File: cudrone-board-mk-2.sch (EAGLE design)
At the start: 58 parts, among them Q1 BSS138, U1 EDISON_CONNECTOR_FULLMOUNTING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, U2 FTS31XS-U, U4 TPS62065, U5 USD-SOCKETNEW, U6 TXB0108, U8 PCA9306, U9 MIC5205

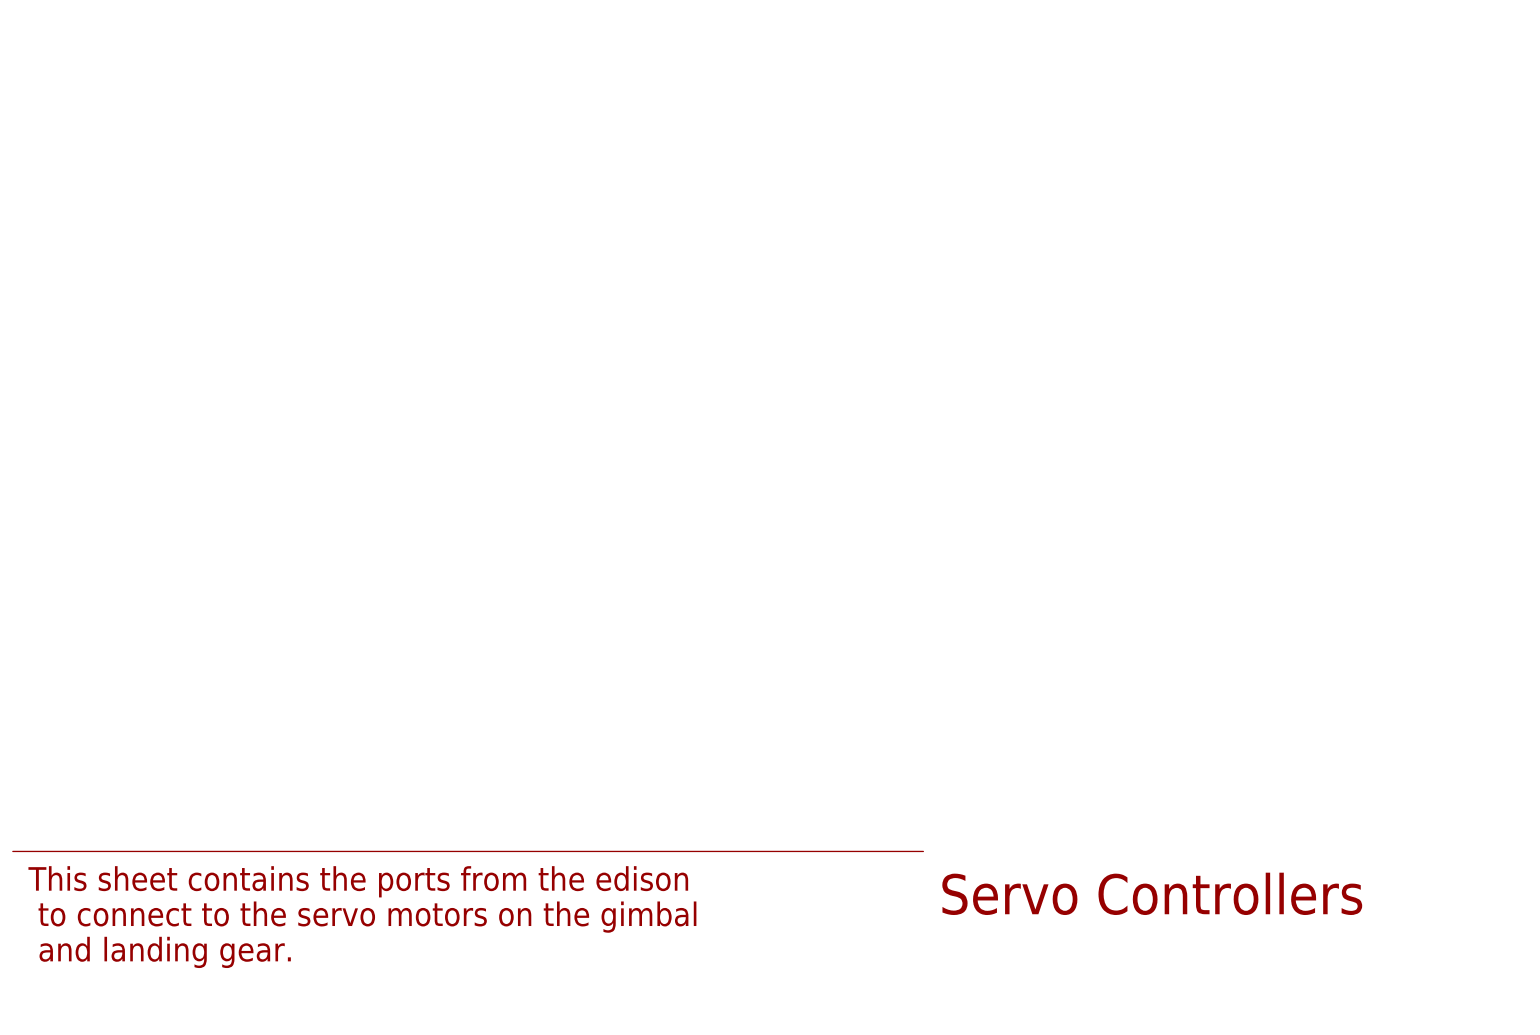
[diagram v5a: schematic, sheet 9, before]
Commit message: Added connectors to schematic
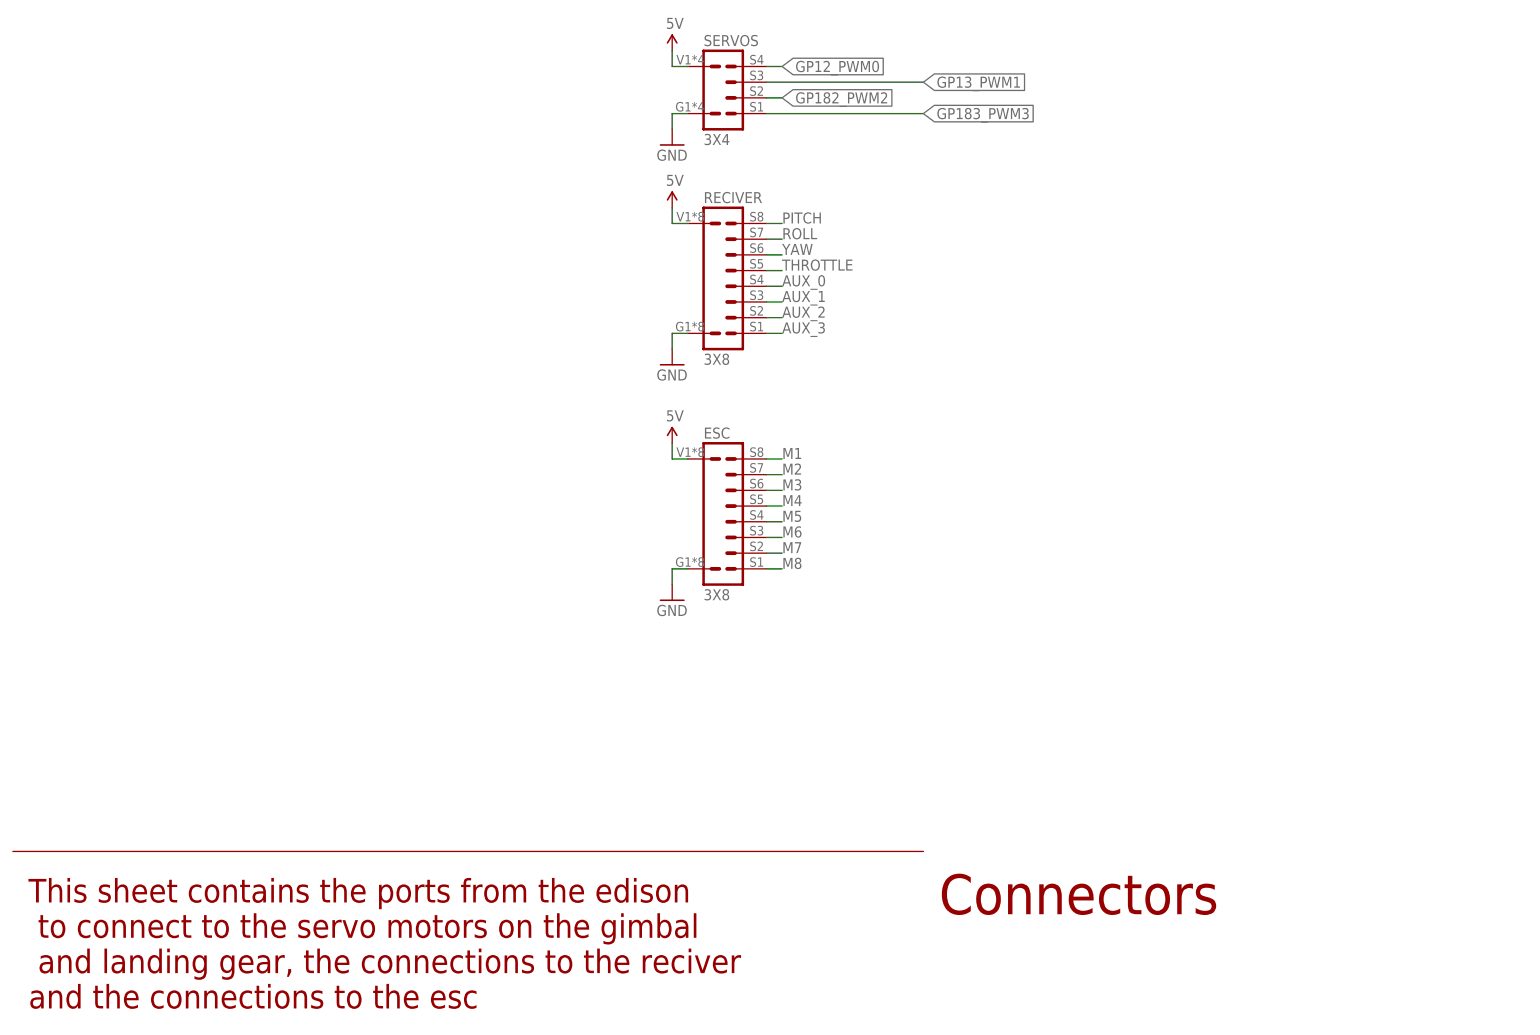
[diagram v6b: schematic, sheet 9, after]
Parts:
- added ESC, RECIVER: 3X8, Drone_Connectors:3X8
- added SERVOS: 3X4, Drone_Connectors:3X4
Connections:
- new net AUX_0: RECIVER.4
- new net AUX_1: RECIVER.3
- new net AUX_2: RECIVER.2
- new net AUX_3: RECIVER.1
- new net M1: ESC.8
- new net M2: ESC.7
- new net M3: ESC.6
- new net M4: ESC.5
- new net M5: ESC.4
- new net M6: ESC.3
- new net M7: ESC.2
- new net M8: ESC.1
- new net PITCH: RECIVER.8
- new net ROLL: RECIVER.7
- new net THROTTLE: RECIVER.5
- new net YAW: RECIVER.6
- net 5V: now also ESC.V, RECIVER.V, SERVOS.V
- net GND: now also ESC.G, RECIVER.G, SERVOS.G
- net GP12_PWM0: now also SERVOS.S4
- net GP13_PWM1: now also SERVOS.S3
- net GP182_PWM2: now also SERVOS.S2
- net GP183_PWM3: now also SERVOS.S1
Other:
- note added: "Connectors"
- note added: "This sheet contains the ports from the edison to connect to the servo motors on the gimbal and landing gear, the connections to the reciver and the connections to the esc"
- note removed: "Servo Controllers"
- note removed: "This sheet contains the ports from the edison to connect to the servo motors on the gimbal and landing gear."
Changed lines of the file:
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@@
 <layer number="113" name="IDFDebug" color="7" fill="1" visible="yes" active="yes"/>
 <layer number="114" name="Badge_Outline" color="11" fill="1" visible="no" active="no"/>
+<layer number="115" name="ReferenceISLANDS" color="7" fill="1" visible="yes" active="yes"/>
 <layer number="116" name="Patch_BOT" color="9" fill="4" visible="yes" active="yes"/>
 <layer number="118" name="Rect_Pads" color="7" fill="1" visible="yes" active="yes"/>
@@
 <part name="SUPPLY22" library="SparkFun-Aesthetics" deviceset="1.8V" device=""/>
 <part name="SUPPLY23" library="SparkFun-Aesthetics" deviceset="1.8V" device=""/>
+<part name="SERVOS" library="Drone_Connectors" deviceset="3X4" device=""/>
+<part name="RECIVER" library="Drone_Connectors" deviceset="3X8" device=""/>
+<part name="ESC" library="Drone_Connectors" deviceset="3X8" device=""/>
+<part name="SUPPLY24" library="SparkFun-Aesthetics" deviceset="5V" device=""/>
+<part name="SUPPLY25" library="SparkFun-Aesthetics" deviceset="5V" device=""/>
+<part name="SUPPLY26" library="SparkFun-Aesthetics" deviceset="5V" device=""/>
+<part name="GND34" library="SparkFun-Aesthetics" deviceset="GND" device=""/>
+<part name="GND35" library="SparkFun-Aesthetics" deviceset="GND" device=""/>
+<part name="GND36" library="SparkFun-Aesthetics" deviceset="GND" device=""/>
 </parts>
 <sheets>
@@
 <sheet>
 <plain>
-<text x="149.86" y="25.4" size="6.4516" layer="94">Servo Controllers</text>
+<text x="149.86" y="25.4" size="6.4516" layer="94">Connectors</text>
 <wire x1="147.32" y1="35.56" x2="0" y2="35.56" width="0.1524" layer="94"/>
-<text x="2.54" y="17.78" size="3.81" layer="94">This sheet contains the ports from the edison
+<text x="2.54" y="10.16" size="3.81" layer="94">This sheet contains the ports from the edison
  to connect to the servo motors on the gimbal
- and landing gear.</text>
+ and landing gear, the connections to the reciver
+and the connections to the esc</text>
 </plain>
 <instances>
 <instance part="FRAME9" gate="G$1" x="0" y="0"/>
 <instance part="FRAME9" gate="G$2" x="147.32" y="0"/>
+<instance part="SERVOS" gate="G$1" x="114.3" y="160.02"/>
+<instance part="RECIVER" gate="G$1" x="114.3" y="129.54"/>
+<instance part="ESC" gate="G$1" x="114.3" y="91.44"/>
+<instance part="SUPPLY24" gate="G$1" x="106.68" y="165.1"/>
+<instance part="SUPPLY25" gate="G$1" x="106.68" y="139.7"/>
+<instance part="SUPPLY26" gate="G$1" x="106.68" y="101.6"/>
+<instance part="GND34" gate="1" x="106.68" y="76.2"/>
+<instance part="GND35" gate="1" x="106.68" y="114.3"/>
+<instance part="GND36" gate="1" x="106.68" y="149.86"/>
 </instances>
 <busses>
 </busses>
 <nets>
+<net name="GND" class="0">
+<segment>
+<pinref part="GND36" gate="1" pin="GND"/>
+<wire x1="106.68" y1="152.4" x2="106.68" y2="154.94" width="0.1524" layer="91"/>
+<pinref part="SERVOS" gate="G$1" pin="G"/>
+<wire x1="106.68" y1="154.94" x2="109.22" y2="154.94" width="0.1524" layer="91"/>
+</segment>
+<segment>
+<pinref part="GND35" gate="1" pin="GND"/>
+<wire x1="106.68" y1="116.84" x2="106.68" y2="119.38" width="0.1524" layer="91"/>
+<pinref part="RECIVER" gate="G$1" pin="G"/>
+<wire x1="106.68" y1="119.38" x2="109.22" y2="119.38" width="0.1524" layer="91"/>
+</segment>
+<segment>
+<pinref part="GND34" gate="1" pin="GND"/>
+<wire x1="106.68" y1="78.74" x2="106.68" y2="81.28" width="0.1524" layer="91"/>
+<pinref part="ESC" gate="G$1" pin="G"/>
+<wire x1="106.68" y1="81.28" x2="109.22" y2="81.28" width="0.1524" layer="91"/>
+</segment>
+</net>
+<net name="5V" class="0">
+<segment>
+<pinref part="SUPPLY24" gate="G$1" pin="5V"/>
+<wire x1="106.68" y1="165.1" x2="106.68" y2="162.56" width="0.1524" layer="91"/>
+<pinref part="SERVOS" gate="G$1" pin="V"/>
+<wire x1="106.68" y1="162.56" x2="109.22" y2="162.56" width="0.1524" layer="91"/>
+</segment>
+<segment>
+<pinref part="SUPPLY25" gate="G$1" pin="5V"/>
+<wire x1="106.68" y1="139.7" x2="106.68" y2="137.16" width="0.1524" layer="91"/>
+<pinref part="RECIVER" gate="G$1" pin="V"/>
+<wire x1="106.68" y1="137.16" x2="109.22" y2="137.16" width="0.1524" layer="91"/>
+</segment>
+<segment>
+<pinref part="SUPPLY26" gate="G$1" pin="5V"/>
+<wire x1="106.68" y1="101.6" x2="106.68" y2="99.06" width="0.1524" layer="91"/>
+<pinref part="ESC" gate="G$1" pin="V"/>
+<wire x1="106.68" y1="99.06" x2="109.22" y2="99.06" width="0.1524" layer="91"/>
+</segment>
+</net>
+<net name="GP12_PWM0" class="0">
+<segment>
+<pinref part="SERVOS" gate="G$1" pin="S4"/>
+<wire x1="121.92" y1="162.56" x2="124.46" y2="162.56" width="0.1524" layer="91"/>
+<label x="124.46" y="162.56" size="1.778" layer="95" xref="yes"/>
+</segment>
+</net>
+<net name="GP13_PWM1" class="0">
+<segment>
+<pinref part="SERVOS" gate="G$1" pin="S3"/>
+<wire x1="121.92" y1="160.02" x2="147.32" y2="160.02" width="0.1524" layer="91"/>
+<label x="147.32" y="160.02" size="1.778" layer="95" xref="yes"/>
+</segment>
+</net>
+<net name="GP182_PWM2" class="0">
+<segment>
+<pinref part="SERVOS" gate="G$1" pin="S2"/>
+<wire x1="121.92" y1="157.48" x2="124.46" y2="157.48" width="0.1524" layer="91"/>
+<label x="124.46" y="157.48" size="1.778" layer="95" xref="yes"/>
+</segment>
+</net>
+<net name="PITCH" class="0">
+<segment>
+<pinref part="RECIVER" gate="G$1" pin="8"/>
+<wire x1="121.92" y1="137.16" x2="124.46" y2="137.16" width="0.1524" layer="91"/>
+<label x="124.46" y="137.16" size="1.778" layer="95"/>
+</segment>
+</net>
+<net name="GP183_PWM3" class="0">
+<segment>
+<pinref part="SERVOS" gate="G$1" pin="S1"/>
+<wire x1="121.92" y1="154.94" x2="147.32" y2="154.94" width="0.1524" layer="91"/>
+<label x="147.32" y="154.94" size="1.778" layer="95" xref="yes"/>
+</segment>
+</net>
+<net name="ROLL" class="0">
+<segment>
+<pinref part="RECIVER" gate="G$1" pin="7"/>
+<wire x1="121.92" y1="134.62" x2="124.46" y2="134.62" width="0.1524" layer="91"/>
+<label x="124.46" y="134.62" size="1.778" layer="95"/>
+</segment>
+</net>
+<net name="YAW" class="0">
+<segment>
+<pinref part="RECIVER" gate="G$1" pin="6"/>
+<wire x1="121.92" y1="132.08" x2="124.46" y2="132.08" width="0.1524" layer="91"/>
+<label x="124.46" y="132.08" size="1.778" layer="95"/>
+</segment>
+</net>
+<net name="THROTTLE" class="0">
+<segment>
+<pinref part="RECIVER" gate="G$1" pin="5"/>
+<wire x1="121.92" y1="129.54" x2="124.46" y2="129.54" width="0.1524" layer="91"/>
+<label x="124.46" y="129.54" size="1.778" layer="95"/>
+</segment>
+</net>
+<net name="AUX_0" class="0">
+<segment>
+<pinref part="RECIVER" gate="G$1" pin="4"/>
+<wire x1="121.92" y1="127" x2="124.46" y2="127" width="0.1524" layer="91"/>
+<label x="124.46" y="127" size="1.778" layer="95"/>
+</segment>
+</net>
+<net name="AUX_1" class="0">
+<segment>
+<pinref part="RECIVER" gate="G$1" pin="3"/>
+<wire x1="121.92" y1="124.46" x2="124.46" y2="124.46" width="0.1524" layer="91"/>
+<label x="124.46" y="124.46" size="1.778" layer="95"/>
+</segment>
+</net>
+<net name="AUX_2" class="0">
+<segment>
+<pinref part="RECIVER" gate="G$1" pin="2"/>
+<wire x1="121.92" y1="121.92" x2="124.46" y2="121.92" width="0.1524" layer="91"/>
+<label x="124.46" y="121.92" size="1.778" layer="95"/>
+</segment>
+</net>
+<net name="AUX_3" class="0">
+<segment>
+<pinref part="RECIVER" gate="G$1" pin="1"/>
+<wire x1="121.92" y1="119.38" x2="124.46" y2="119.38" width="0.1524" layer="91"/>
+<label x="124.46" y="119.38" size="1.778" layer="95"/>
+</segment>
+</net>
+<net name="M1" class="0">
+<segment>
+<pinref part="ESC" gate="G$1" pin="8"/>
+<wire x1="121.92" y1="99.06" x2="124.46" y2="99.06" width="0.1524" layer="91"/>
+<label x="124.46" y="99.06" size="1.778" layer="95"/>
+</segment>
+</net>
+<net name="M2" class="0">
+<segment>
+<pinref part="ESC" gate="G$1" pin="7"/>
+<wire x1="121.92" y1="96.52" x2="124.46" y2="96.52" width="0.1524" layer="91"/>
+<label x="124.46" y="96.52" size="1.778" layer="95"/>
+</segment>
+</net>
+<net name="M3" class="0">
+<segment>
+<pinref part="ESC" gate="G$1" pin="6"/>
+<wire x1="124.46" y1="93.98" x2="121.92" y2="93.98" width="0.1524" layer="91"/>
+<label x="124.46" y="93.98" size="1.778" layer="95"/>
+</segment>
+</net>
+<net name="M4" class="0">
+<segment>
+<pinref part="ESC" gate="G$1" pin="5"/>
+<wire x1="121.92" y1="91.44" x2="124.46" y2="91.44" width="0.1524" layer="91"/>
+<label x="124.46" y="91.44" size="1.778" layer="95"/>
+</segment>
+</net>
+<net name="M5" class="0">
+<segment>
+<pinref part="ESC" gate="G$1" pin="4"/>
+<wire x1="121.92" y1="88.9" x2="124.46" y2="88.9" width="0.1524" layer="91"/>
+<label x="124.46" y="88.9" size="1.778" layer="95"/>
+</segment>
+</net>
+<net name="M6" class="0">
+<segment>
+<pinref part="ESC" gate="G$1" pin="3"/>
+<wire x1="121.92" y1="86.36" x2="124.46" y2="86.36" width="0.1524" layer="91"/>
+<label x="124.46" y="86.36" size="1.778" layer="95"/>
+</segment>
+</net>
+<net name="M7" class="0">
+<segment>
+<pinref part="ESC" gate="G$1" pin="2"/>
+<wire x1="121.92" y1="83.82" x2="124.46" y2="83.82" width="0.1524" layer="91"/>
+<label x="124.46" y="83.82" size="1.778" layer="95"/>
+</segment>
+</net>
+<net name="M8" class="0">
+<segment>
+<pinref part="ESC" gate="G$1" pin="1"/>
+<wire x1="121.92" y1="81.28" x2="124.46" y2="81.28" width="0.1524" layer="91"/>
+<label x="124.46" y="81.28" size="1.778" layer="95"/>
+</segment>
+</net>
 </nets>
 </sheet>
